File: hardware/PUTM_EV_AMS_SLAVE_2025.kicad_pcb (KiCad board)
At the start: 4 copper layers, 100 x 30 mm, 74 parts, among them CN1 4x100nF, CN3 4x100nF, CN5 4x100nF, CN7 4x100nF, IC1 LTC6804HG-1#PBF, J1 TST-110-01-T-D, J2 M80-5100442, J4 M80-5100442, Q1 BCP56, SW1 SW_DIP_x02

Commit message: pending
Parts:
- IC1: moved to B.Cu
- J1: footprint Connector_IDC:IDC-Header_2x09_P2.54mm_Vertical -> Connector_IDC:IDC-Header_2x10_P2.54mm_Vertical_SMD
- moved REF** 53.0 mm to (103.5, 126.5)
- moved IC1 43.0 mm to (150.0, 120.0)
- moved J2 41.2 mm to (192.0, 126.0), turned to 180 degrees
- moved REF** 40.0 mm to (196.5, 113.5)
- moved J1 29.6 mm to (150.0, 120.0)
- moved J4 29.3 mm to (108.0, 114.0), turned to 0 degrees
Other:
- board size 100 x 30 mm -> 100 x 60 mm

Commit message: layout done
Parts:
- removed C12, C9: 10nF/1kV, Capacitor_SMD:C_1206_3216Metric
- removed CN1, CN3, CN5: 4x100nF, Resistor_SMD:R_Array_Convex_4x0603
- removed J4: M80-5100442, Samacsys:M80-51004YY
- removed JP1, JP2: MES, Jumper:SolderJumper-2_P1.3mm_Bridged2Bar_RoundedPad1.0x1.5mm
- removed R57: 100, Resistor_SMD:R_0603_1608Metric
- removed the REF** at (103.5, 96.5)
- removed the REF** at (196.5, 96.5)
- removed RN1, RN3, RN5: 4x100, Resistor_SMD:R_Array_Convex_4x0603
- removed SW1: SW_DIP_x02, Button_Switch_SMD:SW_DIP_SPSTx02_Slide_6.7x6.64mm_W6.73mm_P2.54mm_LowProfile_JPin
- added C7: 4.7nF/Y2, Samacsys:CAPC5728X280N, B.Cu at (191.0, 122.0)
- added C8: 4.7nF/Y2, Samacsys:CAPC5728X280N, B.Cu at (191.0, 118.0)
- added J3: B02B-PASK-1, Samacsys:B02BPASK1LFSN, F.Cu at (196.4, 120.0)
- added REF**: MountingHole_3.2mm_M3, MountingHole:MountingHole_3.2mm_M3, F.Cu at (103.5, 113.5)
- added REF**: MountingHole_3.2mm_M3, MountingHole:MountingHole_3.2mm_M3, F.Cu at (196.5, 126.5)
- C1, C18, C19, C2, C3, C4, CN7, R12, R2, R20, R4, R5, R7, R8, RN7: moved to B.Cu
- C5, C6: value 10nF/1kV -> 4.7nF/Y2; footprint Capacitor_SMD:C_1206_3216Metric -> Samacsys:CAPC5728X280N; moved to B.Cu
- J2: value M80-5100442 -> B02B-PASK-1; footprint Samacsys:M80-51004YY -> Samacsys:B02BPASK1LFSN
- R1, R13, R17, R21, R25, R29, R33, R37, R41, R44, R45, R9: value 68/2W -> 100/1W; footprint Resistor_SMD:R_2512_6332Metric -> Resistor_SMD:R_1210_3225Metric; moved to F.Cu
- moved R44 169.5 mm to (183.0, 125.5), turned to -90 degrees
- moved R1 169.5 mm to (177.2, 125.5)
- moved R9 165.5 mm to (183.0, 116.5)
- moved R10 165.4 mm to (185.5, 115.0), turned to -90 degrees
- moved R48 162.5 mm to (185.5, 124.0), turned to -90 degrees
- moved R14 159.1 mm to (179.8, 115.0), turned to -90 degrees
- moved R45 157.1 mm to (171.5, 125.5), turned to -90 degrees
- moved R13 156.4 mm to (177.2, 116.5)
- moved R46 153.9 mm to (174.0, 124.0), turned to -90 degrees
- moved C3 153.3 mm to (161.0, 125.5), turned to 0 degrees
- moved R18 152.8 mm to (174.0, 115.0), turned to -90 degrees
- moved R17 147.6 mm to (171.5, 116.5)
- moved R6 145.4 mm to (179.8, 124.0), turned to -90 degrees
- moved C18 144.3 mm to (159.0, 114.5)
- moved R5 144.1 mm to (163.0, 114.5)
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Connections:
- net /IMA renamed /IA-
- net /IPA renamed /IA+
- net /L_LTC/IMB renamed /IB-
- net /L_LTC/IPB renamed /IB+
- C6 pad 2: /OUT+ -> /OUT-
- IC1 pad 10: /L_LTC/C8 -> /C8+
- IC1 pad 12: /L_LTC/C7 -> /C7+
- IC1 pad 14: /L_LTC/C6 -> /C6+
- IC1 pad 16: /L_LTC/C5 -> /C5+
- IC1 pad 18: /L_LTC/C4 -> /C4+
- IC1 pad 2: unconnected-(IC1-C12-Pad2) -> /C12+
- IC1 pad 20: /L_LTC/C3 -> /C3+
- IC1 pad 22: /L_LTC/C2 -> /C2+
- IC1 pad 24: /L_LTC/C1 -> /C1+
- IC1 pad 26: /L_LTC/C0 -> /C1-
- IC1 pad 27: /L_LTC/SW_TH1+ -> /TH1+
- IC1 pad 4: /L_LTC/C11 -> /C11+
- IC1 pad 6: /L_LTC/C10 -> /C10+
- IC1 pad 8: /L_LTC/C9 -> /C9+
- J2 pad 2: /OUT+ -> /OUT-
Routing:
- net /C10+: track 0.00 -> 114.8 mm, vias 0 -> 1
- net /C12+: track 0.00 -> 91.1 mm, vias 0 -> 3
- net /L_LTC/S4: track 0.00 -> 69.7 mm, vias 0 -> 1
- net /L_LTC/S5: track 0.00 -> 61.0 mm, vias 0 -> 1
- net /C9+: track 0.00 -> 60.8 mm, vias 0 -> 1
- net /C11+: track 0.00 -> 55.8 mm, vias 0 -> 3
- net /L_LTC/S12: track 0.00 -> 54.7 mm, vias 0 -> 3
- net /C6+: track 0.00 -> 54.0 mm, vias 0 -> 1
- net /C3+: track 0.00 -> 53.1 mm, vias 0 -> 1
- net /L_LTC/S6: track 0.00 -> 50.2 mm, vias 0 -> 1
- net /C5+: track 0.00 -> 49.2 mm, vias 0 -> 1
- net /IA-: track 0.00 -> 49.0 mm
- net /TH1+: track 0.00 -> 48.7 mm, vias 0 -> 3
- net /L_LTC/S9: track 0.00 -> 48.3 mm, vias 0 -> 1
- net /IA+: track 0.00 -> 48.2 mm
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- added copper zone on B.Cu, net /C1-
- added copper zone on F.Cu, net /C1-
- added copper zone on In1.Cu, net /C1-
- added copper zone on In2.Cu, net /C1-
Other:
- board size 100 x 60 mm -> 100 x 20 mm
- board text added: "C1"
- board text added: "C10"
- board text added: "C11"
- board text added: "C12"
- board text added: "C2"
- board text added: "C3"
- board text added: "C4"
- board text added: "C5"
- board text added: "C6"
- board text added: "C7"
- board text added: "C8"
- board text added: "C9"
- board text added: "CONN"
- board text added: "I"
- board text added: "ISO"
- board text added: "LTC"
- board text added: "O"
- board text added: "TMP"

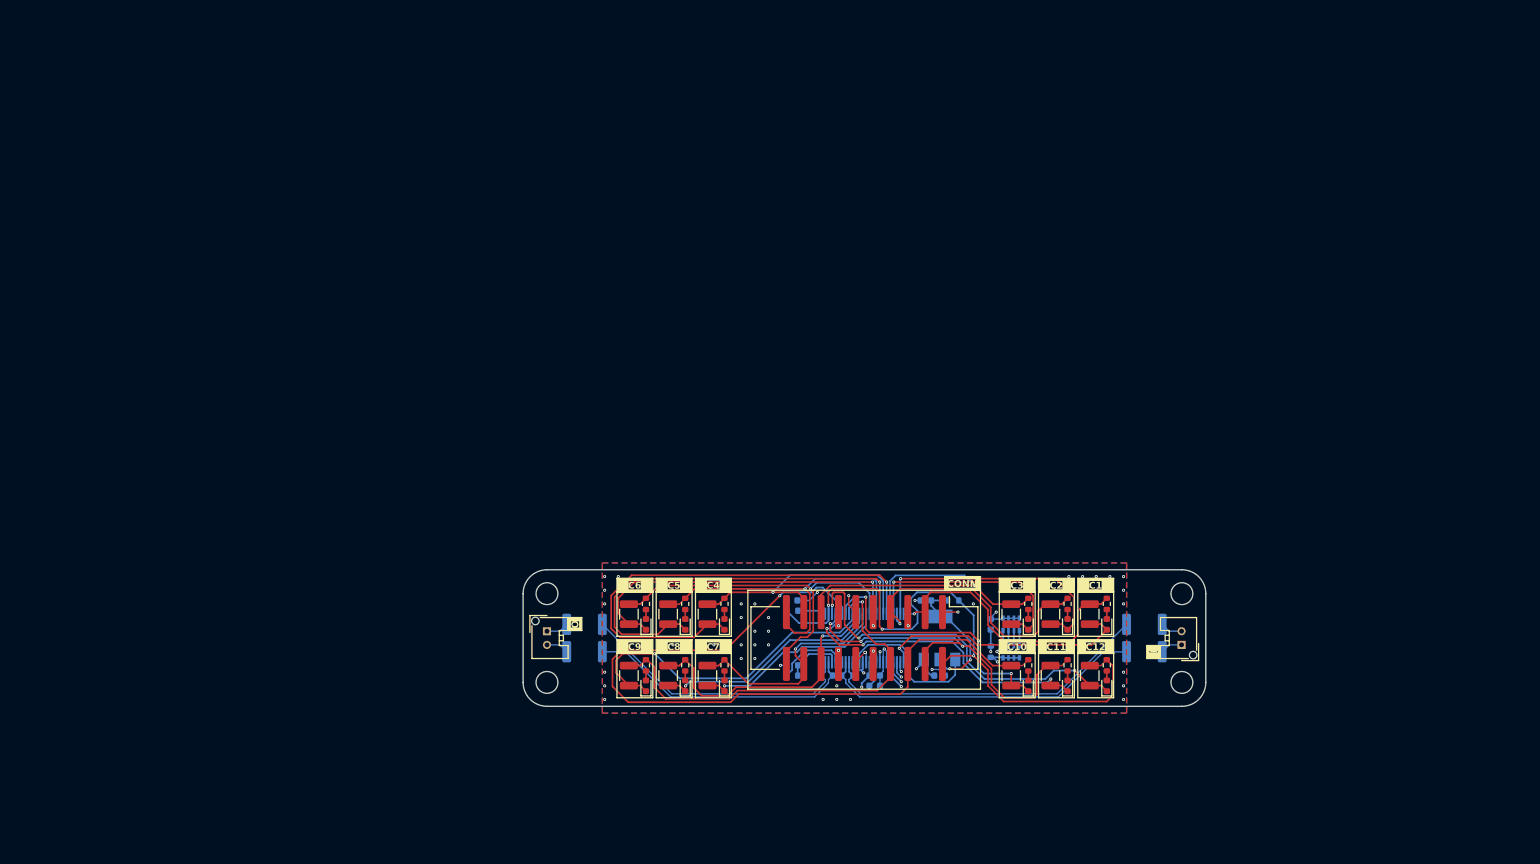
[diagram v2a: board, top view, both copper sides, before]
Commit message: Bq ic balancing and measureing schematic part + main connector
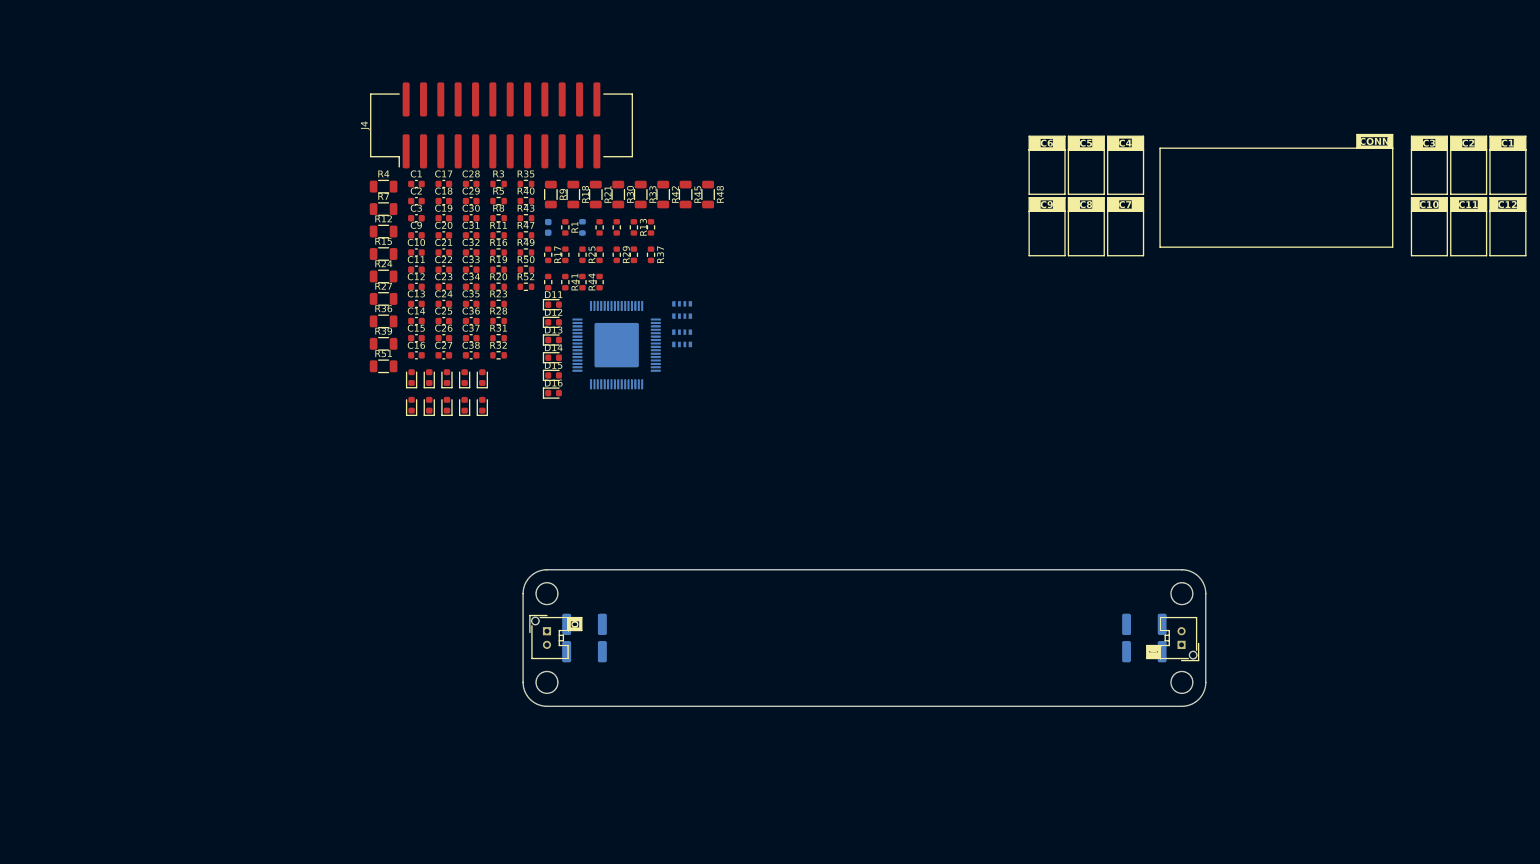
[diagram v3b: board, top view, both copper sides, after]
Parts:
- removed D21, D23: LED, LED_SMD:LED_0603_1608Metric
- removed IC1: LTC6804HG-1#PBF, Samacsys:SOP50P780X200-48N
- removed J1: TST-110-01-T-D, Connector_IDC:IDC-Header_2x10_P2.54mm_Vertical_SMD
- removed Q1: BCP56, Package_TO_SOT_SMD:SOT-223-3_TabPin2
- added C10: 470nF, Capacitor_SMD:C_0603_1608Metric, F.Cu at (84.4, 63.5)
- added C11: 470nF, Capacitor_SMD:C_0603_1608Metric, F.Cu at (84.4, 66.0)
- added C12: 470nF, Capacitor_SMD:C_0603_1608Metric, F.Cu at (84.4, 68.5)
- added C13: 470nF, Capacitor_SMD:C_0603_1608Metric, F.Cu at (84.4, 71.1)
- added C14: 470nF, Capacitor_SMD:C_0603_1608Metric, F.Cu at (84.4, 73.6)
- added C15: 470nF, Capacitor_SMD:C_0603_1608Metric, F.Cu at (84.4, 76.1)
- added C16: 470nF, Capacitor_SMD:C_0603_1608Metric, F.Cu at (84.4, 78.6)
- added C17: 470nF, Capacitor_SMD:C_0603_1608Metric, F.Cu at (88.4, 53.5)
- added C20: 470nF, Capacitor_SMD:C_0603_1608Metric, F.Cu at (88.4, 61.0)
- added C21: 470nF, Capacitor_SMD:C_0603_1608Metric, F.Cu at (88.4, 63.5)
- added C22: 470nF, Capacitor_SMD:C_0603_1608Metric, F.Cu at (88.4, 66.0)
- added C23: 470nF, Capacitor_SMD:C_0603_1608Metric, F.Cu at (88.4, 68.5)
- added C24: 470nF, Capacitor_SMD:C_0603_1608Metric, F.Cu at (88.4, 71.1)
- added C25: 470nF, Capacitor_SMD:C_0603_1608Metric, F.Cu at (88.4, 73.6)
- added C26: 470nF, Capacitor_SMD:C_0603_1608Metric, F.Cu at (88.4, 76.1)
- added C27: 470nF, Capacitor_SMD:C_0603_1608Metric, F.Cu at (88.4, 78.6)
- added C28: 470nF, Capacitor_SMD:C_0603_1608Metric, F.Cu at (92.4, 53.5)
- added C29: 470nF, Capacitor_SMD:C_0603_1608Metric, F.Cu at (92.4, 56.0)
- added C30: 470nF, Capacitor_SMD:C_0603_1608Metric, F.Cu at (92.4, 58.5)
- added C31: 470nF, Capacitor_SMD:C_0603_1608Metric, F.Cu at (92.4, 61.0)
- added C32: 470nF, Capacitor_SMD:C_0603_1608Metric, F.Cu at (92.4, 63.5)
- added C33: 470nF, Capacitor_SMD:C_0603_1608Metric, F.Cu at (92.4, 66.0)
- added C34: 470nF, Capacitor_SMD:C_0603_1608Metric, F.Cu at (92.4, 68.5)
- added C35: 470nF, Capacitor_SMD:C_0603_1608Metric, F.Cu at (92.4, 71.1)
- added C36: 470nF, Capacitor_SMD:C_0603_1608Metric, F.Cu at (92.4, 73.6)
- added C37: 470nF, Capacitor_SMD:C_0603_1608Metric, F.Cu at (92.4, 76.1)
- added C38: 10nF, Capacitor_SMD:C_0603_1608Metric, F.Cu at (92.4, 78.6)
- added C9: 470nF, Capacitor_SMD:C_0603_1608Metric, F.Cu at (84.4, 61.0)
- added D11: LED, LED_SMD:LED_0603_1608Metric, F.Cu at (104.5, 71.2)
- added D12: LED, LED_SMD:LED_0603_1608Metric, F.Cu at (104.5, 73.8)
- added D13: LED, LED_SMD:LED_0603_1608Metric, F.Cu at (104.5, 76.3)
- added D14: LED, LED_SMD:LED_0603_1608Metric, F.Cu at (104.5, 78.9)
- added D15: LED, LED_SMD:LED_0603_1608Metric, F.Cu at (104.5, 81.5)
- added D16: LED, LED_SMD:LED_0603_1608Metric, F.Cu at (104.5, 84.1)
- added IC2: BQ79616PAPR, Samacsys:QFP50P1200X1200X120-65N, B.Cu at (113.7, 77.1)
- added J4: IDC24, Connector_IDC:IDC-Header_2x12_P2.54mm_Vertical_SMD, F.Cu at (96.8, 44.9)
- added R11: 330, Resistor_SMD:R_0603_1608Metric, F.Cu at (96.4, 61.0)
- added R15: 33/1W, Resistor_SMD:R_1206_3216Metric, F.Cu at (79.6, 63.8)
- added R16: 100, Resistor_SMD:R_0603_1608Metric, F.Cu at (96.4, 63.5)
- added R19: 100, Resistor_SMD:R_0603_1608Metric, F.Cu at (96.4, 66.0)
- added R23: 330, Resistor_SMD:R_0603_1608Metric, F.Cu at (96.4, 71.1)
- added R24: 33/1W, Resistor_SMD:R_1206_3216Metric, F.Cu at (79.6, 67.0)
- added R27: 33/1W, Resistor_SMD:R_1206_3216Metric, F.Cu at (79.6, 70.3)
- added R28: 100, Resistor_SMD:R_0603_1608Metric, F.Cu at (96.4, 73.6)
- added R3: 100, Resistor_SMD:R_0603_1608Metric, F.Cu at (96.4, 53.5)
- added R31: 100, Resistor_SMD:R_0603_1608Metric, F.Cu at (96.4, 76.1)
- added R32: 330, Resistor_SMD:R_0603_1608Metric, F.Cu at (96.4, 78.6)
- added R35: 330, Resistor_SMD:R_0603_1608Metric, F.Cu at (100.4, 53.5)
- added R36: 33/1W, Resistor_SMD:R_1206_3216Metric, F.Cu at (79.6, 73.6)
- added R39: 33/1W, Resistor_SMD:R_1206_3216Metric, F.Cu at (79.6, 76.9)
- added R40: 100, Resistor_SMD:R_0603_1608Metric, F.Cu at (100.4, 56.0)
- added R43: 100, Resistor_SMD:R_0603_1608Metric, F.Cu at (100.4, 58.5)
- added R47: 330, Resistor_SMD:R_0603_1608Metric, F.Cu at (100.4, 61.0)
- added R49: 100, Resistor_SMD:R_0603_1608Metric, F.Cu at (100.4, 63.5)
- added R50: 100, Resistor_SMD:R_0603_1608Metric, F.Cu at (100.4, 66.0)
- added R51: 33/1W, Resistor_SMD:R_1206_3216Metric, F.Cu at (79.6, 80.2)
- added R52: 30, Resistor_SMD:R_0603_1608Metric, F.Cu at (100.4, 68.5)
- C1, C2, C3: value 1uF -> 470nF; moved to F.Cu
- C18, C19: value 100nF -> 470nF; moved to F.Cu
- R1, R17, R29, R41, R44: value 100/1W -> 330; footprint Resistor_SMD:R_1210_3225Metric -> Resistor_SMD:R_0603_1608Metric
- R12: value 120 -> 33/1W; footprint Resistor_SMD:R_0603_1608Metric -> Resistor_SMD:R_1206_3216Metric; moved to F.Cu
- R13, R25, R37: value 100/1W -> 100; footprint Resistor_SMD:R_1210_3225Metric -> Resistor_SMD:R_0603_1608Metric
- R18, R30, R42, R48: value 330 -> 33/1W; footprint Resistor_SMD:R_0603_1608Metric -> Resistor_SMD:R_1206_3216Metric
- R20: value 120 -> 330; moved to F.Cu
- R21, R33, R45, R9: value 100/1W -> 33/1W; footprint Resistor_SMD:R_1210_3225Metric -> Resistor_SMD:R_1206_3216Metric
- R22, R34, R46: value 330 -> 100
- R4: value 100 -> 33/1W; footprint Resistor_SMD:R_0603_1608Metric -> Resistor_SMD:R_1206_3216Metric; moved to F.Cu
- R5: moved to F.Cu
- R7: value 1k -> 33/1W; footprint Resistor_SMD:R_0603_1608Metric -> Resistor_SMD:R_1206_3216Metric; moved to F.Cu
- R8: value 1k -> 100; moved to F.Cu
- moved D1 108.1 mm to (83.7, 81.8)
- moved C3 101.8 mm to (84.4, 58.5)
- moved D2 100.2 mm to (86.3, 81.8)
- moved R9 100.0 mm to (104.1, 55.0)
- moved C1 99.5 mm to (84.4, 53.5)
- moved R1 96.7 mm to (106.2, 59.9)
- moved C2 96.6 mm to (84.4, 56.0)
- moved R12 94.0 mm to (79.6, 60.5)
- moved R44 94.0 mm to (108.7, 67.9)
- moved R6 93.9 mm to (111.2, 59.9)
- moved D3 92.5 mm to (88.8, 81.8)
- moved C18 91.7 mm to (88.4, 56.0), turned to 0 degrees
- moved R7 90.8 mm to (79.6, 57.2)
- moved R10 90.5 mm to (113.7, 59.9)
- moved R48 90.4 mm to (127.1, 55.0)
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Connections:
- C1 pad 1: Net-(IC1-VREF2) -> /BQ79616/CB1
- C1 pad 2: /C1- -> /BQ79616/CB0
- C18 pad 1: Net-(Q1-C) -> /BQ79616/VC1
- C18 pad 2: /C1- -> /BQ79616/VC0
- C19 pad 1: /C12+ -> /BQ79616/VC7
- C19 pad 2: /C1- -> /BQ79616/VC6
- C2 pad 1: /L_LTC/VREF2 -> /BQ79616/CB2
- C2 pad 2: /C1- -> /BQ79616/CB1
- C3 pad 1: /L_LTC/VREG -> /BQ79616/VC2
- C3 pad 2: /C1- -> /BQ79616/VC1
- D1 pad 1: /L_LTC/S1 -> /BQ79616/CB1
- D10 pad 1: /L_LTC/S10 -> /BQ79616/CB11
- D2 pad 1: /L_LTC/S2 -> /BQ79616/CB2
- D3 pad 1: /L_LTC/S3 -> /BQ79616/CB3
- D4 pad 1: /L_LTC/S4 -> /BQ79616/CB4
- D5 pad 1: /L_LTC/S5 -> /BQ79616/CB5
- D6 pad 1: /L_LTC/S6 -> /BQ79616/CB6
- D7 pad 1: /L_LTC/S7 -> /BQ79616/CB7
- D8 pad 1: /L_LTC/S8 -> /BQ79616/CB8
- D9 pad 1: /L_LTC/S9 -> /BQ79616/CB9
- R1 pad 1: /C11+ -> /C2+
- R1 pad 2: /L_LTC/S11 -> Net-(D2-A)
- R12 pad 1: /IA+ -> /C4+
- R12 pad 2: /IA- -> /BQ79616/CB4
- R13 pad 1: /C2+ -> /C4+
- R13 pad 2: /L_LTC/S2 -> /BQ79616/VC4
- R14 pad 1: /C2+ -> /C5+
- R14 pad 2: Net-(D2-A) -> Net-(D5-A)
- R17 pad 1: /C3+ -> /C6+
- R17 pad 2: /L_LTC/S3 -> Net-(D6-A)
- R18 pad 1: /C3+ -> /C6+
- R18 pad 2: Net-(D3-A) -> /BQ79616/CB6
- R2 pad 2: /L_LTC/VREF2 -> /BQ79616/VREF2
- R20 pad 1: /IB+ -> /C7+
- R20 pad 2: /IB- -> Net-(D7-A)
- R21 pad 1: /C4+ -> /C7+
- R21 pad 2: /L_LTC/S4 -> /BQ79616/CB7
- R22 pad 1: /C4+ -> /C7+
- R22 pad 2: Net-(D4-A) -> /BQ79616/VC7
- R25 pad 1: /C5+ -> /C8+
- R25 pad 2: /L_LTC/S5 -> /BQ79616/VC8
- R26 pad 1: /C5+ -> /C9+
- R26 pad 2: Net-(D5-A) -> Net-(D9-A)
- R29 pad 1: /C6+ -> /C10+
- R29 pad 2: /L_LTC/S6 -> Net-(D10-A)
- R30 pad 1: /C6+ -> /C10+
- R30 pad 2: Net-(D6-A) -> /BQ79616/CB11
- R33 pad 1: /C7+ -> /C11+
- R33 pad 2: /L_LTC/S7 -> /BQ79616/CB11
- R34 pad 1: /C7+ -> /C11+
- R34 pad 2: Net-(D7-A) -> /BQ79616/VC11
- R37 pad 1: /C8+ -> /C12+
- R37 pad 2: /L_LTC/S8 -> /BQ79616/VC12
- R38 pad 1: /C8+ -> /BQ79616/C13+
- R38 pad 2: Net-(D8-A) -> Net-(D13-A)
- R4 pad 1: Net-(IC1-V+) -> /C2+
- R4 pad 2: /C12+ -> /BQ79616/CB2
- R41 pad 1: /C9+ -> /BQ79616/C14+
- R41 pad 2: /L_LTC/S9 -> Net-(D14-A)
- R42 pad 1: /C9+ -> /BQ79616/C14+
- R42 pad 2: Net-(D9-A) -> /BQ79616/CB14
- R44 pad 1: /C12+ -> /BQ79616/C15+
- R44 pad 2: /L_LTC/S12 -> Net-(D15-A)
- R45 pad 1: /C10+ -> /BQ79616/C15+
- R45 pad 2: /L_LTC/S10 -> /BQ79616/CB15
- R46 pad 1: /C10+ -> /BQ79616/C15+
- R46 pad 2: Net-(D10-A) -> /BQ79616/VC15
- R48 pad 1: /C12+ -> /BQ79616/C16+
- R48 pad 2: Net-(D23-A) -> /BQ79616/CB16
- R5 pad 1: /C12+ -> /C2+
- R5 pad 2: Net-(Q1-C) -> /BQ79616/VC2
- R6 pad 1: /C11+ -> /C3+
- R6 pad 2: Net-(D21-A) -> Net-(D3-A)
- R7 pad 1: Net-(IC1-IBIAS) -> /C3+
- R7 pad 2: Net-(IC1-ICMP) -> /BQ79616/CB3
- R8 pad 1: Net-(IC1-ICMP) -> /C3+
- R8 pad 2: /C1- -> /BQ79616/VC3
- R9 pad 2: /L_LTC/S1 -> /BQ79616/CB1
- RN7 pad 5: /L_LTC/VREF2 -> /BQ79616/VREF2
- RN7 pad 6: /L_LTC/VREF2 -> /BQ79616/VREF2
- RN7 pad 7: /L_LTC/VREF2 -> /BQ79616/VREF2
- RN7 pad 8: /L_LTC/VREF2 -> /BQ79616/VREF2
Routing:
- net /C10+: track 114.8 -> 0.00 mm, vias 1 -> 0
- net /C12+: track 91.1 -> 0.00 mm, vias 3 -> 0
- net /L_LTC/S4: track 69.7 -> 0.00 mm, vias 1 -> 0
- net /L_LTC/S5: track 61.0 -> 0.00 mm, vias 1 -> 0
- net /C9+: track 60.8 -> 0.00 mm, vias 1 -> 0
- net /C11+: track 55.8 -> 0.00 mm, vias 3 -> 0
- net /L_LTC/S12: track 54.7 -> 0.00 mm, vias 3 -> 0
- net /C6+: track 54.0 -> 0.00 mm, vias 1 -> 0
- net /C3+: track 53.1 -> 0.00 mm, vias 1 -> 0
- net /L_LTC/S6: track 50.2 -> 0.00 mm, vias 1 -> 0
- net /C5+: track 49.2 -> 0.00 mm, vias 1 -> 0
- net /IA-: track 49.0 -> 0.00 mm
- net /TH1+: track 48.7 -> 0.00 mm, vias 3 -> 0
- net /L_LTC/S9: track 48.3 -> 0.00 mm, vias 1 -> 0
- net /IA+: track 48.2 -> 0.00 mm
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- removed copper zone on B.Cu, net /C1-
- removed copper zone on F.Cu, net /C1-
- removed copper zone on In1.Cu, net /C1-
- removed copper zone on In2.Cu, net /C1-

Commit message: sync
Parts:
- added C39: 10nF, Capacitor_SMD:C_0603_1608Metric, F.Cu at (139.3, 34.9)
- added C40: 1uF, Capacitor_SMD:C_0603_1608Metric, F.Cu at (139.3, 37.5)
- added C41: 100nF, Capacitor_SMD:C_0603_1608Metric, F.Cu at (139.3, 40.0)
- added C42: 1uF, Capacitor_SMD:C_0603_1608Metric, F.Cu at (139.3, 42.5)
- added C43: 1uF, Capacitor_SMD:C_0603_1608Metric, F.Cu at (139.3, 45.0)
- added C44: 1uF, Capacitor_SMD:C_0603_1608Metric, F.Cu at (139.3, 47.5)
- added C45: 1uF, Capacitor_SMD:C_0603_1608Metric, F.Cu at (139.3, 50.0)
- added C46: 220pF, Capacitor_SMD:C_0603_1608Metric, F.Cu at (143.3, 34.9)
- added C47: 220pF, Capacitor_SMD:C_0603_1608Metric, F.Cu at (143.3, 37.5)
- added C48: 220pF, Capacitor_SMD:C_0603_1608Metric, F.Cu at (143.3, 40.0)
- added C49: 220pF, Capacitor_SMD:C_0603_1608Metric, F.Cu at (143.3, 42.5)
- added L1: 100-500uH, Inductor_SMD:L_CommonModeChoke_Coilcraft_1812CAN, F.Cu at (139.8, 56.7)
- added L2: 100-500uH, Inductor_SMD:L_CommonModeChoke_Coilcraft_1812CAN, F.Cu at (144.6, 56.7)
- added Q2: 100V/2W, Package_TO_SOT_SMD:SOT-223-3_TabPin2, F.Cu at (154.2, 37.9)
- added R53: 100, Resistor_SMD:R_0603_1608Metric, F.Cu at (143.3, 45.0)
- added R54: 200, Resistor_SMD:R_0603_1608Metric, F.Cu at (143.3, 47.5)
- added R55: 1k, Resistor_SMD:R_0603_1608Metric, F.Cu at (143.3, 50.0)
- added R56: 49, Resistor_SMD:R_0603_1608Metric, F.Cu at (147.3, 34.9)
- added R57: 49, Resistor_SMD:R_0603_1608Metric, F.Cu at (147.3, 37.5)
- added R58: 1k, Resistor_SMD:R_0603_1608Metric, F.Cu at (147.3, 40.0)
- added R59: 49, Resistor_SMD:R_0603_1608Metric, F.Cu at (147.3, 42.5)
- added R60: 49, Resistor_SMD:R_0603_1608Metric, F.Cu at (147.3, 45.0)
- C1, C10, C11, C12, C13, C14, C15, C16, C17, C18, C19, C2, C20, C21, C22, C23, C24, C25, C26, C27, C28, C29, C3, C30, C31, C32, C33, C34, C35, C36, C37, C9: value 470nF -> 470nF/16V
- C38: value 10nF -> 10nF/100V
- moved R51 131.6 mm to (210.0, 97.9)
- moved C1 122.5 mm to (203.5, 81.9), turned to -90 degrees
- moved C18 118.1 mm to (202.7, 85.6), turned to 180 degrees
- moved D1 116.1 mm to (199.7, 85.6), turned to 0 degrees
- moved R4 114.3 mm to (189.1, 86.4), turned to 180 degrees
- moved C3 111.4 mm to (190.6, 92.0), turned to -90 degrees
- moved R3 110.6 mm to (202.7, 84.1), turned to 180 degrees
- moved R7 108.5 mm to (184.0, 86.4), turned to 180 degrees
- moved C2 108.4 mm to (187.6, 89.0), turned to -90 degrees
- moved C37 106.7 mm to (195.7, 102.8), turned to -90 degrees
- moved C10 105.1 mm to (185.5, 92.0), turned to -90 degrees
- moved C36 103.7 mm to (192.7, 99.8), turned to -90 degrees
- moved D2 103.3 mm to (189.1, 92.0)
- moved C35 103.2 mm to (190.6, 102.8), turned to -90 degrees
- moved R12 102.7 mm to (178.9, 86.4), turned to 180 degrees
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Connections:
- net /BQ79616/VREF2 renamed Net-(RN7-R1.2)
- C24 pad 1: /BQ79616/CB11 -> /BQ79616/CB10
- C26 pad 2: /BQ79616/CB11 -> /BQ79616/CB10
- C38 pad 1: /C1- -> /BQ79616/C1-
- D10 pad 1: /BQ79616/CB11 -> /BQ79616/CB10
- IC2 pad 14: /BQ79616/CB11 -> /BQ79616/CB10
- IC2 pad 36: unconnected-(IC2-REFHM-Pad36) -> /BQ79616/C1-
- IC2 pad 37: unconnected-(IC2-REFHP-Pad37) -> Net-(IC2-REFHP)
- IC2 pad 38: unconnected-(IC2-AVDD-Pad38) -> Net-(IC2-AVDD)
- IC2 pad 39: unconnected-(IC2-AVSS-Pad39) -> /BQ79616/C1-
- IC2 pad 40: unconnected-(IC2-COMLP-Pad40) -> Net-(IC2-COMLP)
- IC2 pad 41: unconnected-(IC2-COMLN-Pad41) -> Net-(IC2-COMLN)
- IC2 pad 42: unconnected-(IC2-COMHN-Pad42) -> Net-(IC2-COMHN)
- IC2 pad 43: unconnected-(IC2-COMHP-Pad43) -> Net-(IC2-COMHP)
- IC2 pad 44: unconnected-(IC2-NEG5V-Pad44) -> Net-(IC2-NEG5V)
- IC2 pad 45: unconnected-(IC2-CVDD-Pad45) -> Net-(IC2-CVDD)
- IC2 pad 46: unconnected-(IC2-CVSS-Pad46) -> /BQ79616/C1-
- IC2 pad 47: unconnected-(IC2-LDOIN-Pad47) -> Net-(IC2-LDOIN)
- IC2 pad 48: unconnected-(IC2-BBP_1-Pad48) -> Net-(IC2-NPNB)
- IC2 pad 49: unconnected-(IC2-DVDD-Pad49) -> Net-(IC2-DVDD)
- IC2 pad 50: unconnected-(IC2-DVSS-Pad50) -> /BQ79616/C1-
- IC2 pad 51: unconnected-(IC2-TSREF-Pad51) -> /BQ79616/TSREF
- IC2 pad 63: unconnected-(IC2-BBN-Pad63) -> /C8+
- IC2 pad 64: unconnected-(IC2-BBP_2-Pad64) -> /C9+
- IC2 pad 65: /C1- -> /BQ79616/C1-
- J2 pad 1: /OUT+ -> Net-(J2-Pin_1)
- J2 pad 2: /OUT- -> Net-(J2-Pin_2)
- J3 pad 1: /IN+ -> Net-(J3-Pin_1)
- J3 pad 2: /IN- -> Net-(J3-Pin_2)
- R30 pad 2: /BQ79616/CB11 -> /BQ79616/CB10
- R38 pad 1: /BQ79616/C13+ -> /C13+
- R39 pad 1: /BQ79616/C13+ -> /C13+
- R40 pad 1: /BQ79616/C13+ -> /C13+
- R41 pad 1: /BQ79616/C14+ -> /C14+
- R42 pad 1: /BQ79616/C14+ -> /C14+
- R43 pad 1: /BQ79616/C14+ -> /C14+
- R44 pad 1: /BQ79616/C15+ -> /C15+
- R45 pad 1: /BQ79616/C15+ -> /C15+
- R46 pad 1: /BQ79616/C15+ -> /C15+
- R47 pad 1: /BQ79616/C16+ -> /C16+
- R48 pad 1: /BQ79616/C16+ -> /C16+
- R49 pad 1: /BQ79616/C16+ -> /C16+
- R52 pad 1: /C1- -> /C16+
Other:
- board text added: "C13"
- board text added: "C14"
- board text added: "C15"
- board text added: "C16"
